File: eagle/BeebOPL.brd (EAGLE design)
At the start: 100 x 80 mm, 31 parts, among them IC1 LM324N, IC2 YM3014B, IC3 74LS00N, IC4 74LS27N, IC5 74LS02N, IC6 YM3812, IC7 74LS04N, J1 1 MHz Bus, J2 Feed-through, J3 3.5mm Jack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

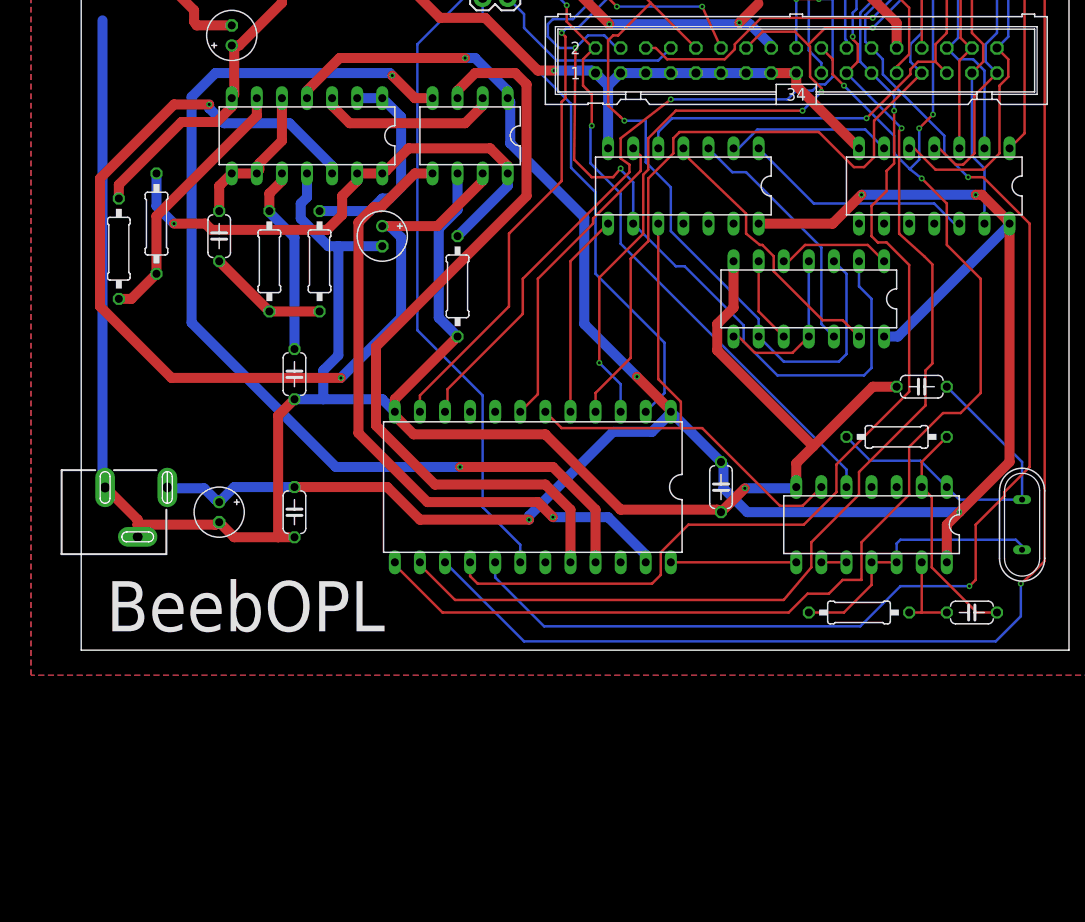
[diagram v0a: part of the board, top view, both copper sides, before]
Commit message: Replaced 74LS27 with 74HCT688
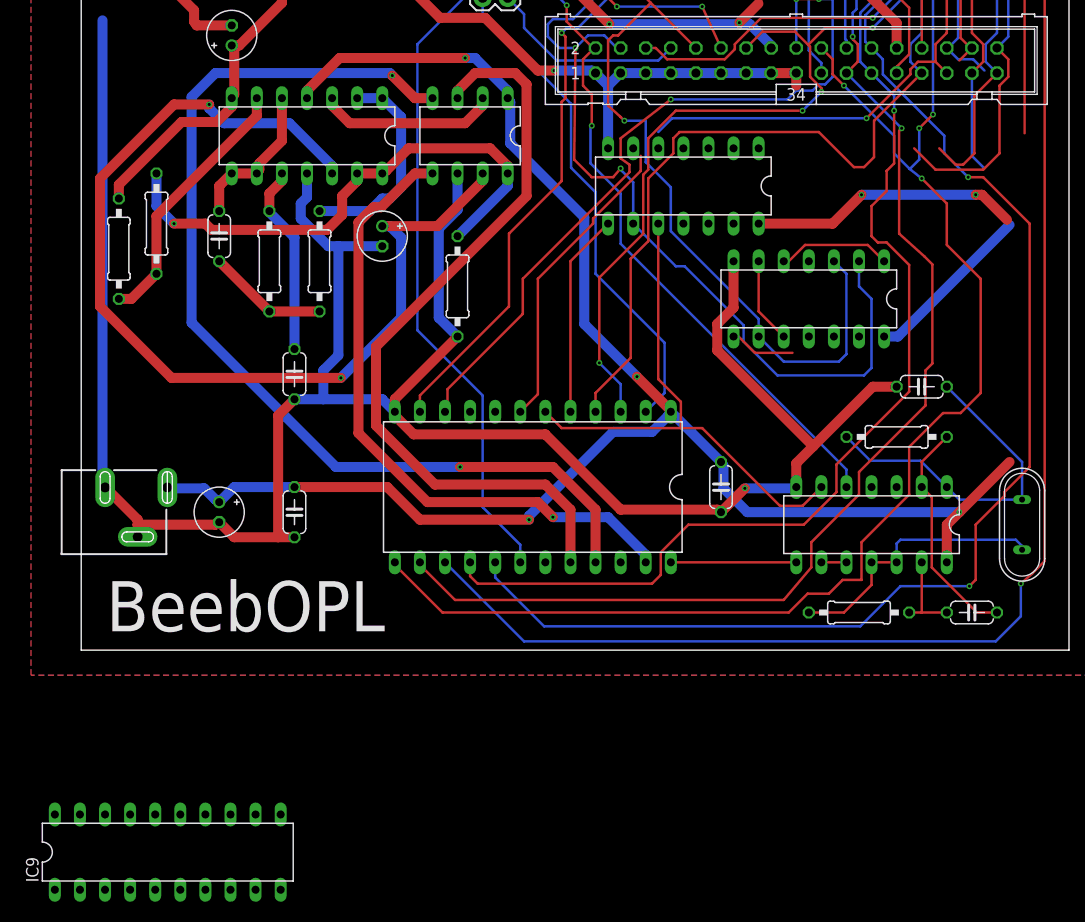
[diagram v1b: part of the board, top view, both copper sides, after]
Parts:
- removed IC4: 74LS27N, 74xx-us:DIL14
- added IC9: 74HCT688N, 74xx-eu:DIL20
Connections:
- removed net N$14: IC3.3, IC5.12
- removed net N$2: IC3.1, IC4.12
- removed net N$23: IC3.4, IC5.13
- removed net N$3: IC3.2, IC4.6
- net A1: now also IC9.4; no longer IC4.1
- net A2: now also IC9.6; no longer IC3.5
- net A3: now also IC9.8; no longer IC4.2
- net A4: now also IC9.11; no longer IC4.13
- net A5: now also IC9.13; no longer IC4.3
- net A6: now also IC9.15; no longer IC4.4
- net A7: now also IC9.17; no longer IC4.5
- net CNPGFC: now also IC9.2; no longer IC5.11
- net GND: now also IC9.1, IC9.10, IC9.12, IC9.14, IC9.16, IC9.18, IC9.3, IC9.5, IC9.9; no longer IC4.7
- net N$30: now also IC9.19; no longer IC3.6
- net VCC: now also IC9.20, IC9.7; no longer IC4.14
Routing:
- net N$23: track 27.9 -> 0.00 mm
- net N$14: track 25.1 -> 0.00 mm
- net VCC: track 238.6 -> 213.9 mm
- net N$2: track 23.5 -> 0.00 mm
- net N$3: track 16.8 -> 0.00 mm
- net CNPGFC: track 16.6 -> 6.65 mm
- net GND: track 424.2 -> 415.2 mm
- net A5: track 24.4 -> 15.5 mm
- net A3: track 26.4 -> 18.5 mm
- net A4: track 29.4 -> 23.8 mm
- net A1: track 48.0 -> 45.8 mm
- net A2: track 46.6 -> 45.0 mm
- net N$30: track 32.0 -> 31.0 mm
- net A7: track 35.9 -> 35.4 mm
- net A6: track 27.9 -> 27.4 mm

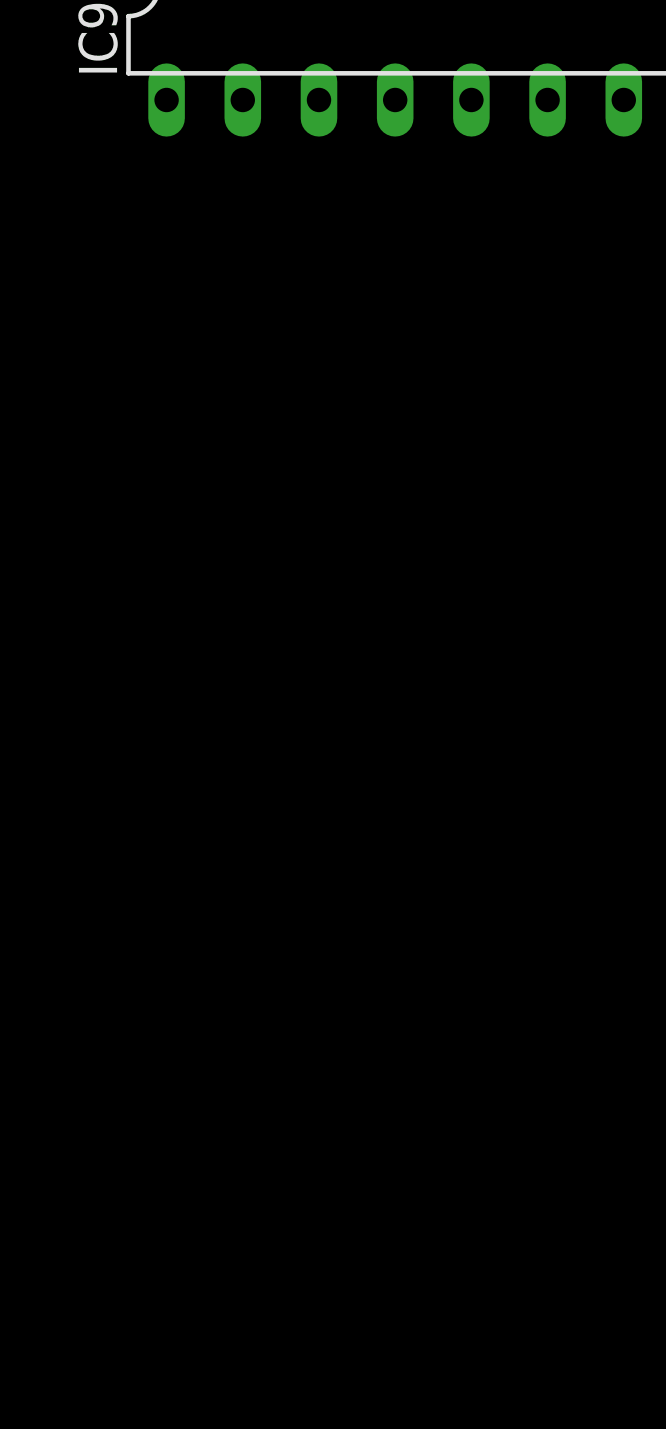
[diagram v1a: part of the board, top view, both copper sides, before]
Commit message: Added mounting holes
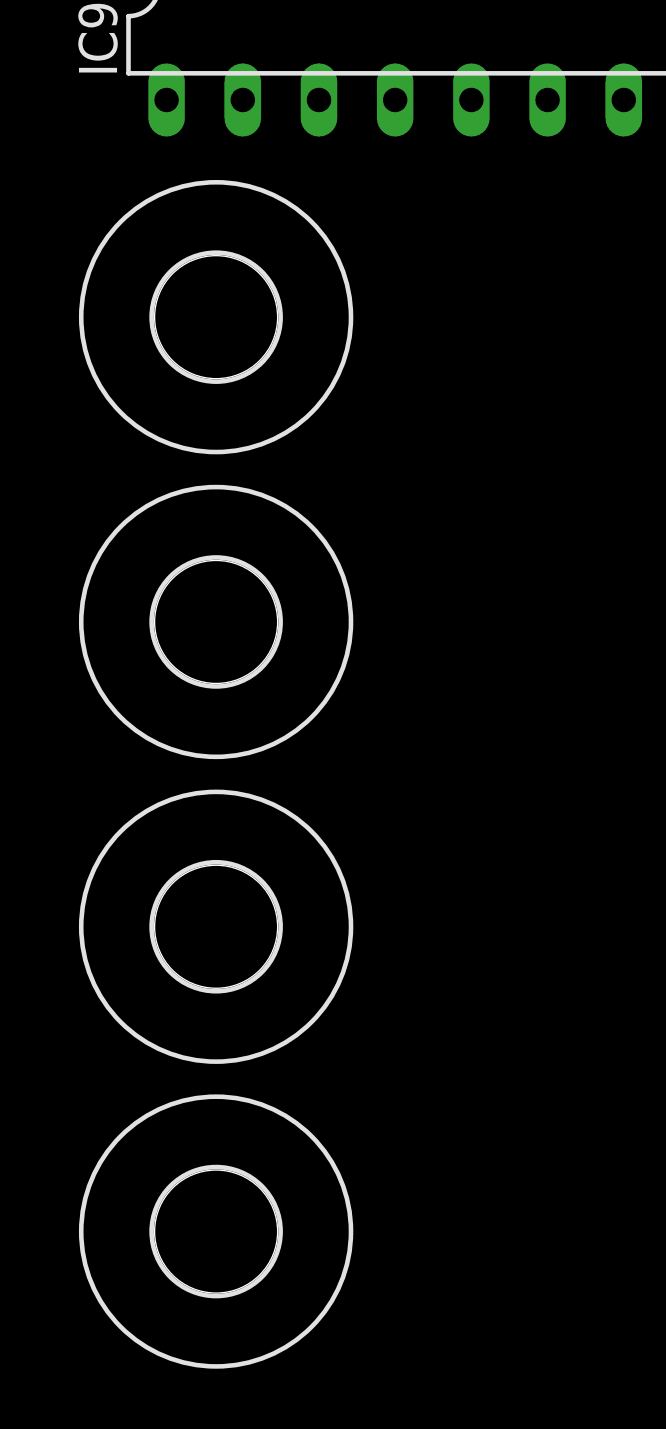
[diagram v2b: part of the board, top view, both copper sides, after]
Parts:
- added H1, H2, H3, H4: MOUNT-HOLE4.1, holes:4,1
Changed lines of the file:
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@@
 </element>
 <element name="IC9" library="74xx-eu" package="DIL20" value="74HCT688N" x="8.763" y="-20.447"/>
+<element name="H1" library="holes" package="4,1" value="MOUNT-HOLE4.1" x="-1.016" y="-31.496"/>
+<element name="H2" library="holes" package="4,1" value="MOUNT-HOLE4.1" x="-1.016" y="-41.656"/>
+<element name="H3" library="holes" package="4,1" value="MOUNT-HOLE4.1" x="-1.016" y="-51.816"/>
+<element name="H4" library="holes" package="4,1" value="MOUNT-HOLE4.1" x="-1.016" y="-61.976"/>
 </elements>
 <signals>

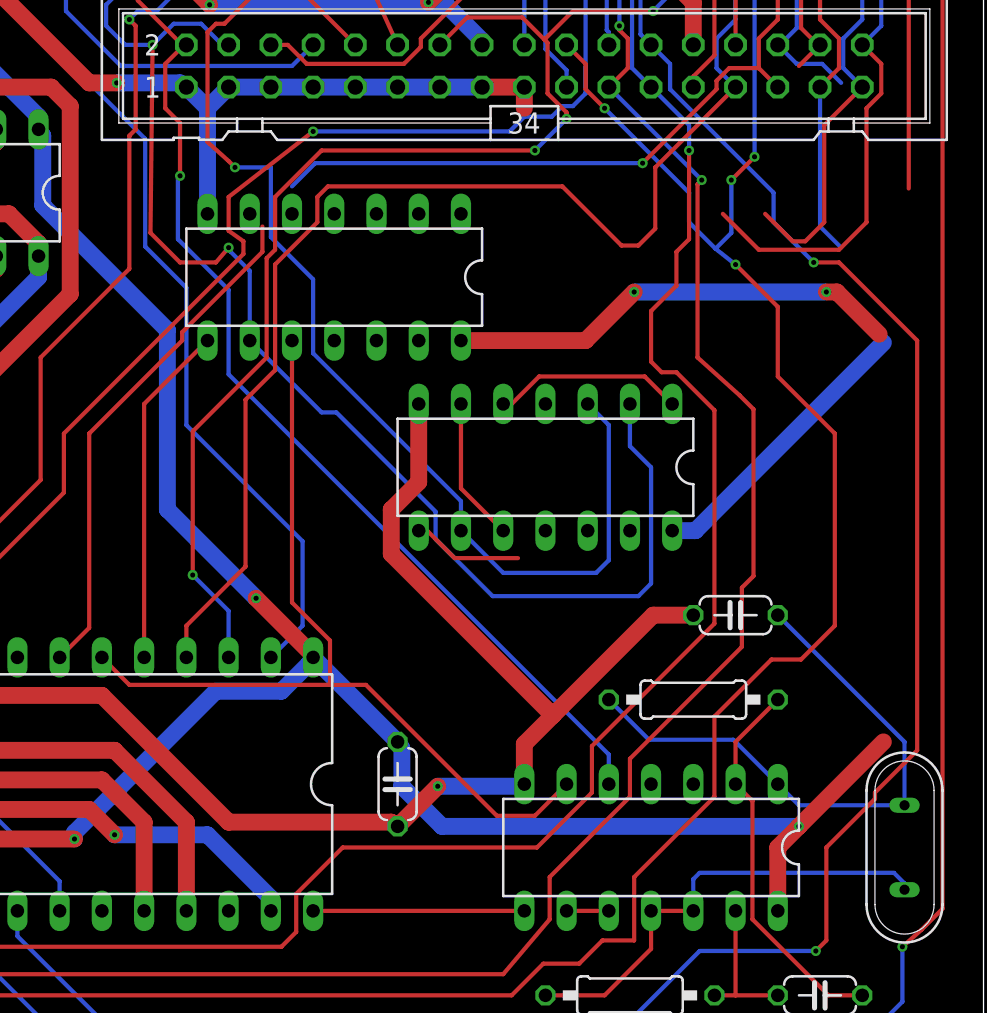
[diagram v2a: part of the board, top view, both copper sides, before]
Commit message: Removed 74LS00
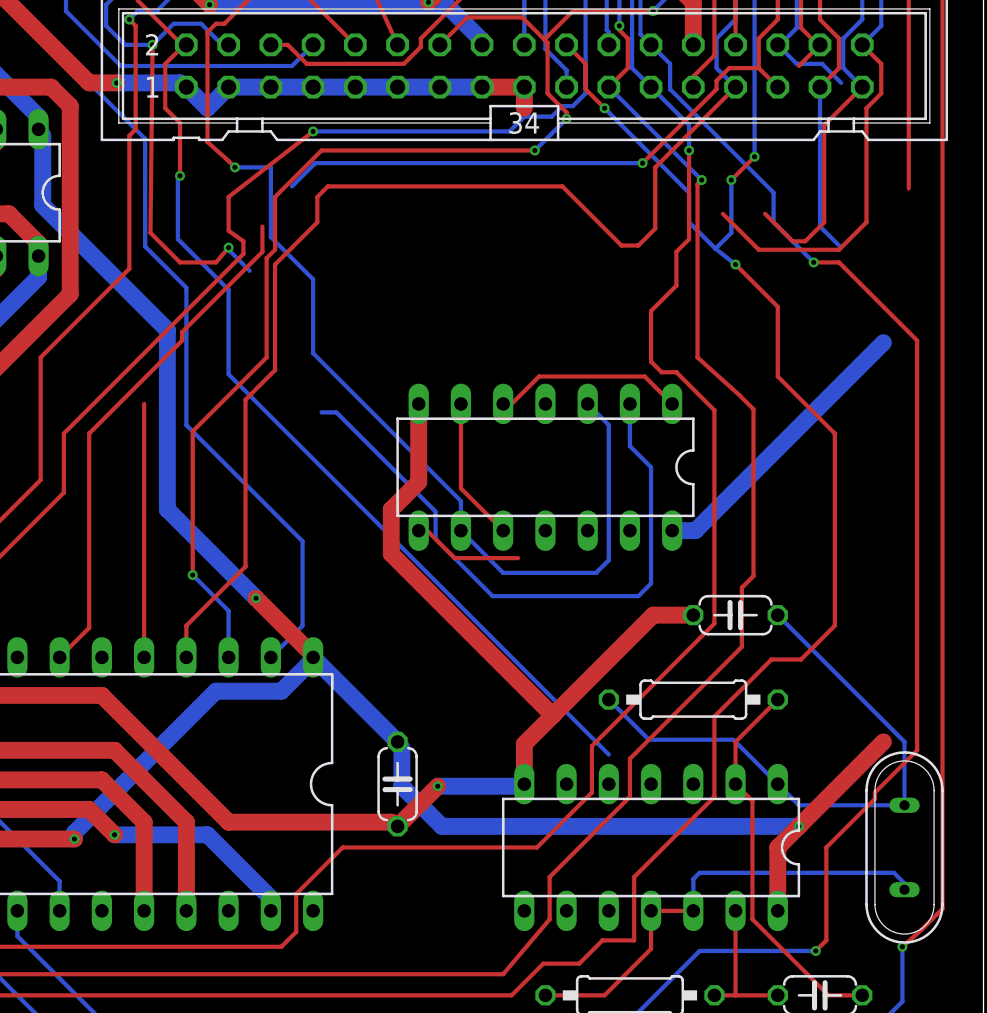
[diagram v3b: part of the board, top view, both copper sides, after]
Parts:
- removed IC3: 74LS00N, 74xx-us:DIL14
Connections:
- removed net /RD: IC3.10, IC6./RD, IC7.6
- removed net N$25: IC6.0M, IC7.8
- new net N$14: IC6./RD, IC7.8
- new net N$2: IC5.13, IC7.3
- new net N$3: IC5.11, IC7.6
- net 1MHZE: now also IC7.5; no longer IC3.9
- net GND: no longer IC3.7
- net N$24: now also IC7.4; no longer IC3.8
- net N$26: now also IC6.0M; no longer IC7.9
- net R/W: now also IC5.12, IC7.9; no longer IC7.5
- net VCC: no longer IC3.14
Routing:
- net /RD: track 54.3 -> 0.00 mm
- net VCC: track 213.9 -> 186.5 mm, vias 6 -> 4
- net N$25: track 12.7 -> 0.00 mm
- net 1MHZE: track 106.2 -> 95.9 mm
- net GND: track 415.2 -> 408.9 mm
- net N$24: track 20.6 -> 15.2 mm
- net N$26: track 2.54 -> 0.00 mm
- net R/W: track 77.6 -> 75.8 mm
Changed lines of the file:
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@@
 <attribute name="VALUE" x="98.298" y="16.51" size="1.27" layer="27" ratio="10" rot="R270"/>
-</element>
-<element name="IC3" library="74xx-us" package="DIL14" value="74LS00N" x="60.96" y="46.99" smashed="yes" rot="R180">
-<attribute name="VALUE" x="64.516" y="47.625" size="1.27" layer="27" ratio="10" rot="R180"/>
 </element>
 <element name="IC7" library="74xx-us" package="DIL14" value="74LS04N" x="80.01" y="12.7" smashed="yes" rot="R180">
@@
 <contactref element="C8" pad="2"/>
 <contactref element="IC2" pad="GND"/>
-<contactref element="IC3" pad="7"/>
 <contactref element="IC7" pad="7"/>
 <contactref element="J2" pad="26"/>
@@
 <wire x1="72.39" y1="58.42" x2="72.39" y2="57.15" width="1.016" layer="1"/>
 <wire x1="72.39" y1="58.42" x2="69.85" y2="58.42" width="1.016" layer="1"/>
-<wire x1="53.34" y1="57.15" x2="53.34" y2="50.8" width="1.016" layer="16"/>
 <wire x1="52.07" y1="58.42" x2="53.34" y2="57.15" width="1.016" layer="16"/>
 <wire x1="53.34" y1="57.15" x2="54.61" y2="58.42" width="1.016" layer="16"/>
@@
 <contactref element="C8" pad="1"/>
 <contactref element="IC2" pad="VDD"/>
-<contactref element="IC3" pad="14"/>
 <contactref element="IC7" pad="14"/>
 <wire x1="22.86" y1="56.642" x2="22.86" y2="55.88" width="1.016" layer="1"/>
@@
 <wire x1="13.589" y1="15.24" x2="13.97" y2="14.986" width="1.016" layer="16"/>
 <wire x1="59.69" y1="24.13" x2="64.77" y2="19.05" width="1.016" layer="16"/>
-<wire x1="76.073" y1="43.18" x2="68.58" y2="43.18" width="1.016" layer="1"/>
-<wire x1="78.994" y1="46.101" x2="76.073" y2="43.18" width="1.016" layer="1"/>
-<wire x1="90.551" y1="46.101" x2="78.994" y2="46.101" width="1.016" layer="16"/>
-<wire x1="91.186" y1="46.101" x2="90.551" y2="46.101" width="1.016" layer="1"/>
-<wire x1="93.726" y1="43.561" x2="91.186" y2="46.101" width="1.016" layer="1"/>
 <wire x1="82.677" y1="31.75" x2="81.28" y2="31.75" width="1.016" layer="16"/>
 <wire x1="93.98" y1="43.053" x2="82.677" y2="31.75" width="1.016" layer="16"/>
@@
 <wire x1="43.434" y1="55.499" x2="43.18" y2="55.88" width="1.016" layer="16"/>
 <via x="38.862" y="59.944" extent="1-16" drill="0.3048"/>
-<via x="78.994" y="46.101" extent="1-16" drill="0.3048"/>
-<via x="90.551" y="46.101" extent="1-16" drill="0.3048"/>
 <via x="88.9" y="13.97" extent="1-16" drill="0.3048"/>
 <via x="45.339" y="13.208" extent="1-16" drill="0.3048"/>
@@
 <contactref element="IC9" pad="20"/>
 <contactref element="IC9" pad="7"/>
-<wire x1="93.98" y1="43.053" x2="93.726" y2="43.561" width="0" layer="19" extent="1-16"/>
 <wire x1="93.98" y1="19.05" x2="82.677" y2="31.75" width="0" layer="19" extent="1-16"/>
 <wire x1="-2.667" y1="-16.637" x2="8.763" y2="16.383" width="0" layer="19" extent="16-16"/>
@@
 <contactref element="IC5" pad="2"/>
 <contactref element="J2" pad="4"/>
-<contactref element="IC3" pad="9"/>
 <wire x1="50.038" y1="60.96" x2="51.308" y2="62.23" width="0.254" layer="16"/>
 <wire x1="48.895" y1="72.39" x2="53.594" y2="67.691" width="0.254" layer="1"/>
@@
 <wire x1="67.056" y1="32.893" x2="67.056" y2="31.242" width="0.254" layer="16"/>
 <wire x1="54.61" y1="48.768" x2="53.848" y2="47.879" width="0.254" layer="1"/>
-<wire x1="55.88" y1="43.18" x2="55.88" y2="47.371" width="0.254" layer="16"/>
 <via x="53.594" y="67.691" extent="1-16" drill="0.3048"/>
 <via x="50.038" y="60.96" extent="1-16" drill="0.3048"/>
@@
 <wire x1="55.88" y1="47.371" x2="54.737" y2="48.514" width="0.254" layer="16"/>
 <wire x1="54.737" y1="48.514" x2="54.61" y2="48.768" width="0.254" layer="16"/>
-<wire x1="55.88" y1="43.18" x2="60.198" y2="38.862" width="0.254" layer="16"/>
 <wire x1="60.198" y1="38.862" x2="61.087" y2="38.862" width="0.254" layer="16"/>
 <wire x1="61.087" y1="38.862" x2="67.056" y2="32.893" width="0.254" layer="16"/>
@@
 <wire x1="49.276" y1="78.867" x2="50.8" y2="78.867" width="0.254" layer="1"/>
 <wire x1="50.8" y1="78.867" x2="54.61" y2="75.057" width="0.254" layer="1"/>
+<contactref element="IC7" pad="5"/>
+<wire x1="60.198" y1="38.862" x2="55.88" y2="47.371" width="0" layer="19" extent="16-16"/>
+<wire x1="77.47" y1="16.51" x2="79.248" y2="27.813" width="0" layer="19" extent="16-16"/>
 </signal>
 <signal name="R/W">
 <contactref element="J1" pad="2"/>
 <contactref element="J2" pad="2"/>
-<contactref element="IC7" pad="5"/>
-<wire x1="77.47" y1="18.288" x2="77.47" y2="16.51" width="0.254" layer="16"/>
 <wire x1="51.943" y1="60.96" x2="50.8" y2="59.817" width="0.254" layer="1"/>
 <wire x1="52.07" y1="60.96" x2="51.943" y2="60.96" width="0.254" layer="1"/>
@@
 <wire x1="54.61" y1="46.228" x2="54.61" y2="41.148" width="0.254" layer="16"/>
 <wire x1="54.61" y1="41.148" x2="77.47" y2="18.288" width="0.254" layer="16"/>
+<contactref element="IC5" pad="12"/>
+<contactref element="IC7" pad="9"/>
+<wire x1="77.47" y1="18.288" x2="76.2" y2="31.75" width="0" layer="19" extent="16-16"/>
+<wire x1="74.93" y1="8.89" x2="77.47" y2="18.288" width="0" layer="19" extent="16-16"/>
 </signal>
 <signal name="CNPGFC">
@@
 <via x="47.752" y="13.462" extent="1-16" drill="0.3048"/>
 </signal>
-<signal name="/RD">
-<contactref element="IC6" pad="/RD"/>
-<contactref element="IC3" pad="10"/>
-<contactref element="IC7" pad="6"/>
-<wire x1="73.025" y1="14.605" x2="74.93" y2="16.51" width="0.254" layer="1"/>
-<wire x1="70.739" y1="14.605" x2="73.025" y2="14.605" width="0.254" layer="1"/>
-<wire x1="62.865" y1="22.479" x2="70.739" y2="14.605" width="0.254" layer="1"/>
-<wire x1="48.641" y1="22.479" x2="60.706" y2="22.479" width="0.254" layer="1"/>
-<wire x1="60.706" y1="22.479" x2="62.865" y2="22.479" width="0.254" layer="1"/>
-<wire x1="46.99" y1="24.13" x2="48.641" y2="22.479" width="0.254" layer="1"/>
-<wire x1="58.42" y1="27.432" x2="58.42" y2="43.18" width="0.254" layer="1"/>
-<wire x1="60.706" y1="25.146" x2="58.42" y2="27.432" width="0.254" layer="1"/>
-<wire x1="60.706" y1="22.479" x2="60.706" y2="25.146" width="0.254" layer="1"/>
-</signal>
 <signal name="N$30">
 <contactref element="IC6" pad="/CS"/>
@@
 </signal>
 <signal name="N$24">
-<contactref element="IC3" pad="8"/>
 <contactref element="IC6" pad="/WR"/>
 <wire x1="49.53" y1="39.37" x2="49.53" y2="24.13" width="0.254" layer="1"/>
-<wire x1="53.34" y1="43.18" x2="49.53" y2="39.37" width="0.254" layer="1"/>
+<contactref element="IC7" pad="4"/>
+<wire x1="49.53" y1="24.13" x2="80.01" y2="16.51" width="0" layer="19" extent="1-1"/>
 </signal>
 <signal name="N$26">
-<contactref element="IC7" pad="9"/>
 <contactref element="IC7" pad="10"/>
-<wire x1="77.47" y1="8.89" x2="74.93" y2="8.89" width="0.254" layer="1"/>
-</signal>
-<signal name="N$25">
+<contactref element="IC6" pad="0M"/>
+<wire x1="59.69" y1="8.89" x2="77.47" y2="8.89" width="0" layer="19" extent="1-1"/>
+</signal>
+<signal name="N$2">
+<contactref element="IC5" pad="13"/>
+<contactref element="IC7" pad="3"/>
+<wire x1="82.55" y1="16.51" x2="78.74" y2="31.75" width="0" layer="19" extent="1-1"/>
+</signal>
+<signal name="N$3">
+<contactref element="IC7" pad="6"/>
+<contactref element="IC5" pad="11"/>
+<wire x1="74.93" y1="16.51" x2="73.66" y2="31.75" width="0" layer="19" extent="1-1"/>
+</signal>
+<signal name="N$14">
 <contactref element="IC7" pad="8"/>
-<contactref element="IC6" pad="0M"/>
-<wire x1="72.39" y1="8.89" x2="59.69" y2="8.89" width="0.254" layer="1"/>
+<contactref element="IC6" pad="/RD"/>
+<wire x1="46.99" y1="24.13" x2="72.39" y2="8.89" width="0" layer="19" extent="1-1"/>
 </signal>
 </signals>
